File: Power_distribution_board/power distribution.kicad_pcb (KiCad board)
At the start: 2 copper layers, 74 x 45 mm, 17 parts, among them J1 Pin headers, J10 XT30 Connector, J2 Pin headers, J3 Pin headers, J4 Pin headers, J6 Pin headers, J7 Pin headers, J8 Pin headers, J9 XT30 Connector, SW2 SW_SPST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

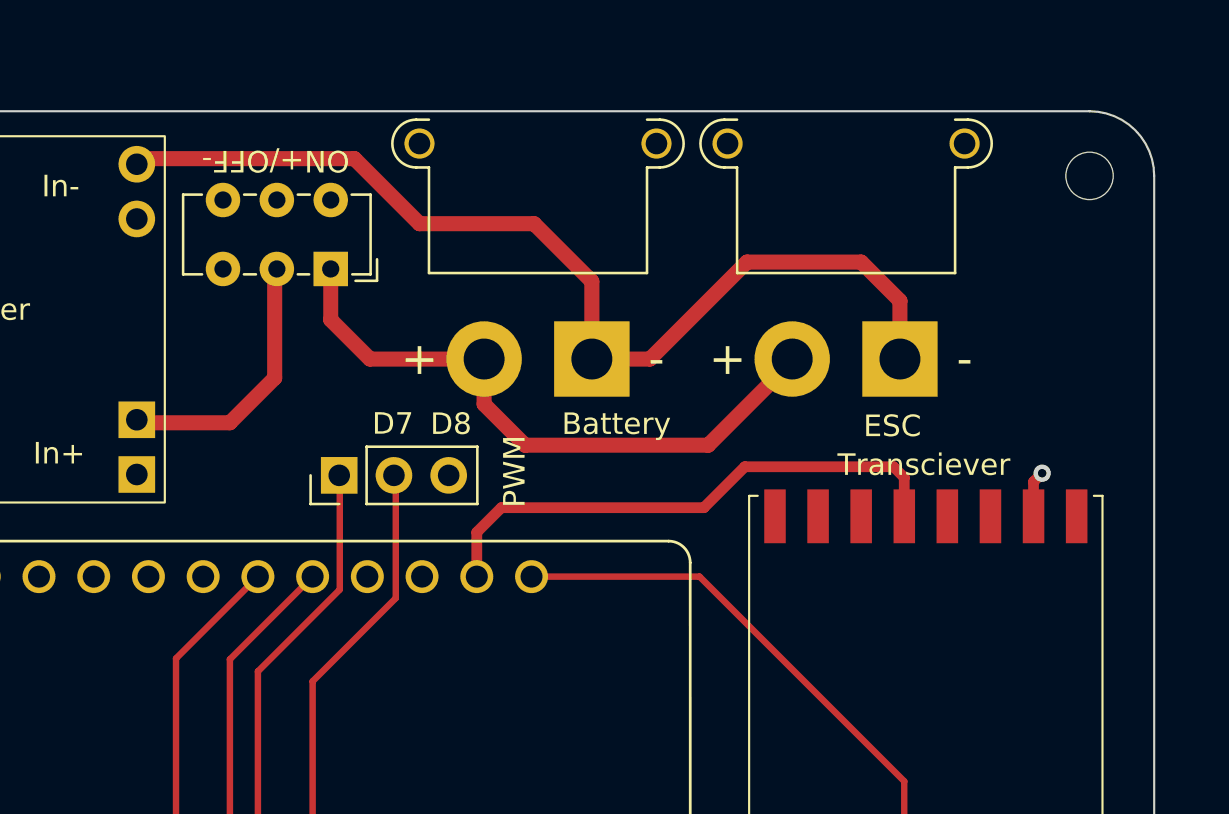
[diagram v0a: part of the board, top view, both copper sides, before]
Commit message: added new switch footprint, update gerbers
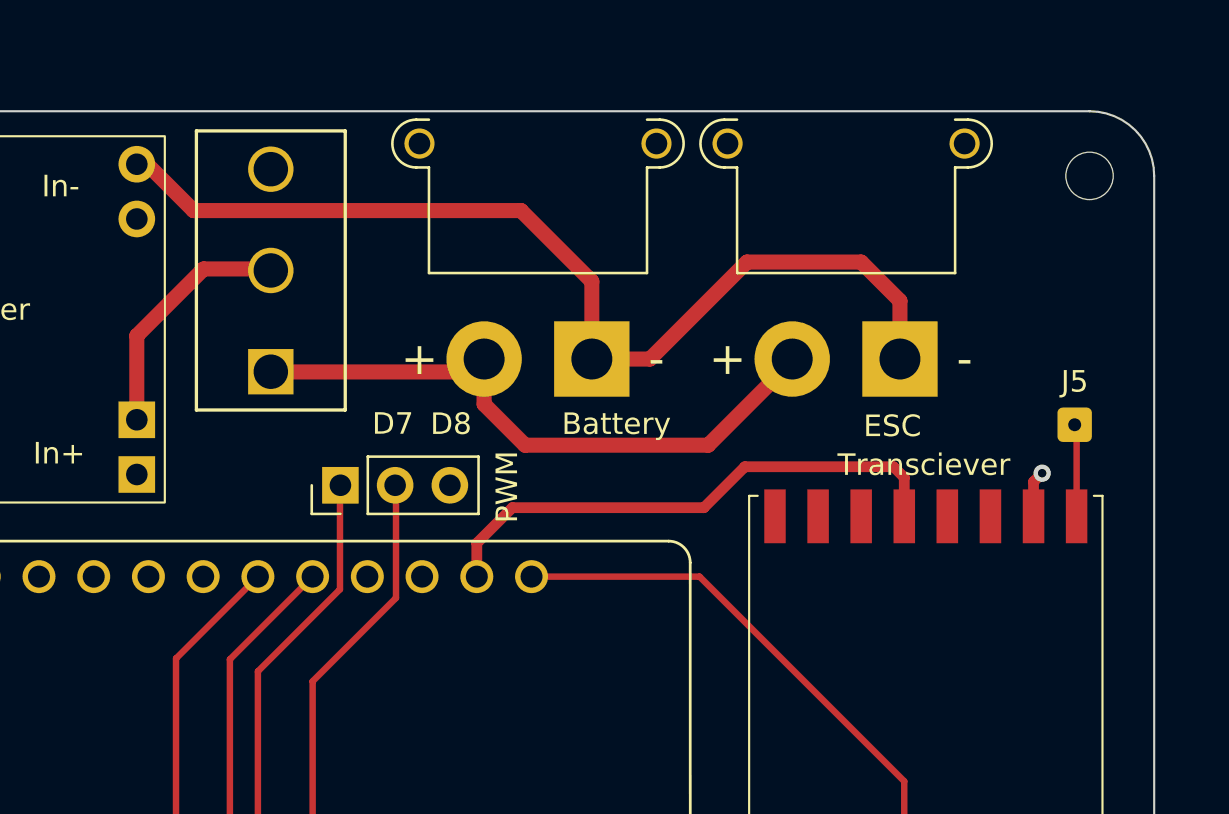
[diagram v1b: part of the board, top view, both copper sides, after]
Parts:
- added J5: Solder pad, Connector_Wire:SolderWire-0.1sqmm_1x01_D0.4mm_OD1mm, F.Cu at (174.3, 79.5)
- SW2: footprint Button_Switch_THT:SW_E-Switch_EG1271_SPDT -> GH36P010001:GH36P010001_APM
- moved SW2 5.52 mm to (137.0, 77.1)
- moved J6 0.46 mm to (140.2, 82.4)
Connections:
- U2 pad 9: unconnected-(U2-ANT-Pad9) -> Net-(J5-Pin_1)
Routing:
- net Net-(J5-Pin_1): track 0.00 -> 4.29 mm

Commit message: update backups
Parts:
- J5: value Solder pad -> Antenna
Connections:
- net Net-(J5-Pin_1) renamed /Antenna
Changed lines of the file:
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@@
 	(net 43 "unconnected-(U1-IN+-Pad7)")
 	(net 44 "Net-(J10-Pin_2)")
-	(net 45 "Net-(J5-Pin_1)")
+	(net 45 "/Antenna")
 	(footprint "MountingHole:MountingHole_2.2mm_M2"
 		(layer "F.Cu")
@@
 				(font
 					(size 1.27 1.27)
+					(thickness 0.15)
 				)
 			)
@@
 				(font
 					(size 1.27 1.27)
+					(thickness 0.15)
 				)
 			)
@@
 				(font
 					(size 1.27 1.27)
+					(thickness 0.15)
 				)
 			)
@@
 				(font
 					(size 1.27 1.27)
+					(thickness 0.15)
 				)
 			)
@@
 				(font
 					(size 1.27 1.27)
+					(thickness 0.15)
 				)
 			)
@@
 				(font
 					(size 1.27 1.27)
+					(thickness 0.15)
 				)
 			)
@@
 				(font
 					(size 1.27 1.27)
+					(thickness 0.15)
 				)
 			)
@@
 				(font
 					(size 1.27 1.27)
+					(thickness 0.15)
 				)
 			)
@@
 				(font
 					(size 1.27 1.27)
+					(thickness 0.15)
 				)
 			)
@@
 				(font
 					(size 1.27 1.27)
+					(thickness 0.15)
 				)
 			)
@@
 				(font
 					(size 1.27 1.27)
+					(thickness 0.15)
 				)
 			)
@@
 				(font
 					(size 1.27 1.27)
+					(thickness 0.15)
 				)
 			)
@@
 				(font
 					(size 1.27 1.27)
+					(thickness 0.15)
 				)
 			)
@@
 				(font
 					(size 1.27 1.27)
+					(thickness 0.15)
 				)
 			)
@@
 				(font
 					(size 1.27 1.27)
+					(thickness 0.15)
 				)
 			)
@@
 				(font
 					(size 1.27 1.27)
+					(thickness 0.15)
 				)
 			)
@@
 				(font
 					(size 1.27 1.27)
+					(thickness 0.15)
 				)
 			)
 		)
-		(property "Description" ""
+		(property "Description" "Generic connector, single row, 01x02, script generated (kicad-library-utils/schlib/autogen/connector/)"
 			(at 0 0 0)
 			(unlocked yes)
@@
 				(font
 					(size 1.27 1.27)
+					(thickness 0.15)
 				)
 			)
@@
 				(font
 					(size 1.27 1.27)
+					(thickness 0.15)
 				)
 			)
@@
 				(font
 					(size 1.27 1.27)
+					(thickness 0.15)
 				)
 			)
 		)
-		(property "Description" ""
+		(property "Description" "Generic connector, single row, 01x02, script generated (kicad-library-utils/schlib/autogen/connector/)"
 			(at 0 0 0)
 			(unlocked yes)
@@
 				(font
 					(size 1.27 1.27)
+					(thickness 0.15)
 				)
 			)
@@
 			)
 		)
-		(property "Value" "Solder pad"
+		(property "Value" "Antenna"
 			(at 0 2 0)
 			(layer "F.Fab")
@@
 				(font
 					(size 1.27 1.27)
+					(thickness 0.15)
 				)
 			)
@@
 				(font
 					(size 1.27 1.27)
+					(thickness 0.15)
 				)
 			)
@@
 				(font
 					(size 1.27 1.27)
+					(thickness 0.15)
 				)
 			)
@@
 			(remove_unused_layers no)
 			(roundrect_rratio 0.15625)
-			(net 45 "Net-(J5-Pin_1)")
+			(net 45 "/Antenna")
 			(pinfunction "Pin_1")
 			(pintype "passive")
@@
 				(font
 					(size 1.27 1.27)
+					(thickness 0.15)
 				)
 			)
@@
 				(font
 					(size 1.27 1.27)
+					(thickness 0.15)
 				)
 			)
@@
 				(font
 					(size 1.27 1.27)
+					(thickness 0.15)
 				)
 			)
@@
 			(size 2.5 1)
 			(layers "F.Cu" "F.Paste" "F.Mask")
-			(net 45 "Net-(J5-Pin_1)")
+			(net 45 "/Antenna")
 			(pinfunction "ANT")
 			(pintype "bidirectional")
@@
 				(font
 					(size 1.27 1.27)
+					(thickness 0.15)
 				)
 			)
@@
 				(font
 					(size 1.27 1.27)
+					(thickness 0.15)
 				)
 			)
@@
 				(font
 					(size 1.27 1.27)
+					(thickness 0.15)
 				)
 			)
@@
 				(font
 					(size 1.27 1.27)
+					(thickness 0.15)
 				)
 			)
@@
 				(font
 					(size 1.27 1.27)
+					(thickness 0.15)
 				)
 			)
@@
 				(font
 					(size 1.27 1.27)
+					(thickness 0.15)
 				)
 			)
@@
 				(font
 					(size 1.27 1.27)
+					(thickness 0.15)
 				)
 			)
@@
 				(font
 					(size 1.27 1.27)
+					(thickness 0.15)
 				)
 			)
@@
 				(font
 					(size 1.27 1.27)
+					(thickness 0.15)
 				)
 			)
@@
 				(font
 					(size 1.27 1.27)
+					(thickness 0.15)
 				)
 			)
@@
 				(font
 					(size 1.27 1.27)
+					(thickness 0.15)
 				)
 			)
@@
 				(font
 					(size 1.27 1.27)
+					(thickness 0.15)
 				)
 			)
@@
 				(font
 					(size 1.27 1.27)
+					(thickness 0.15)
 				)
 			)
@@
 				(font
 					(size 1.27 1.27)
+					(thickness 0.15)
 				)
 			)
@@
 				(font
 					(size 1.27 1.27)
+					(thickness 0.15)
 				)
 			)
@@
 				(font
 					(size 1.27 1.27)
+					(thickness 0.15)
 				)
 			)
@@
 				(font
 					(size 1.27 1.27)
+					(thickness 0.15)
 				)
 			)
@@
 				(font
 					(size 1.27 1.27)
+					(thickness 0.15)
 				)
 			)
@@
 				(font
 					(size 1.27 1.27)
+					(thickness 0.15)
 				)
 			)
@@
 				(font
 					(size 1.27 1.27)
+					(thickness 0.15)
 				)
 			)
@@
 				(font
 					(size 1.27 1.27)
+					(thickness 0.15)
 				)
 			)
@@
 				(font
 					(size 1.27 1.27)
+					(thickness 0.15)
 				)
 			)
@@
 				(font
 					(size 1.27 1.27)
+					(thickness 0.15)
 				)
 			)
@@
 				(font
 					(size 1.27 1.27)
+					(thickness 0.15)
 				)
 			)
